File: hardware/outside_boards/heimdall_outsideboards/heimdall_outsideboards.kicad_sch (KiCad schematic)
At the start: 33 parts, among them IC1 CLRC66303HNY, J1 Motherboard, J2 LED Out, Y1 27.12MHz

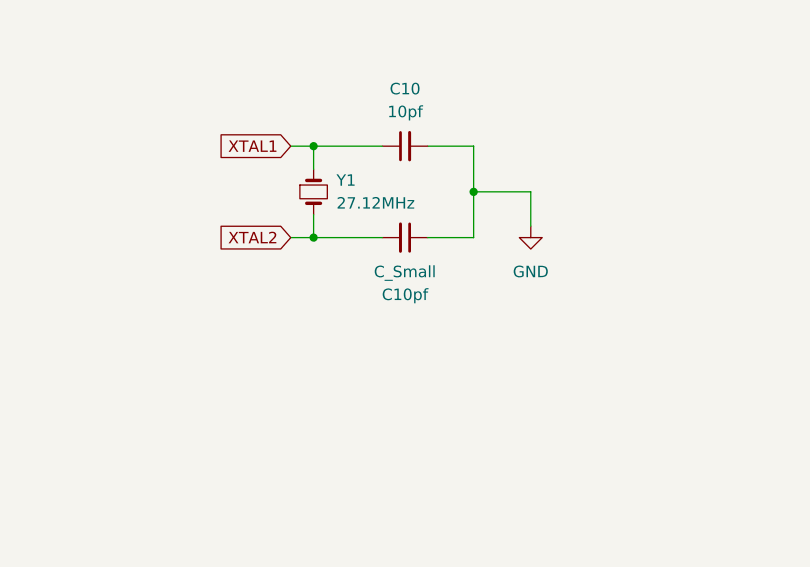
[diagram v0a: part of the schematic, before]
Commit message: Finished adding footprints
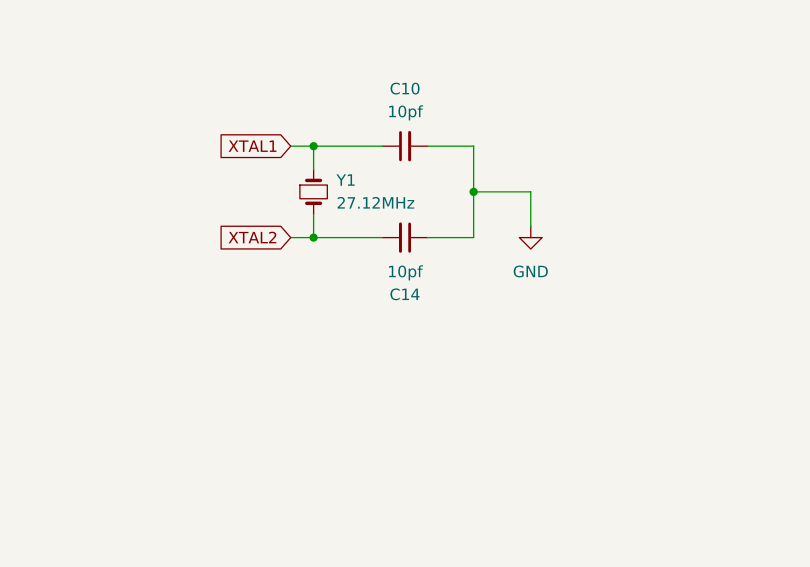
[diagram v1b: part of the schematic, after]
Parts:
- C14: renamed from C10pf; value C_Small -> 10pf
- J1: footprint (none) -> Connector_PinHeader_2.54mm:PinHeader_1x09_P2.54mm_Vertical
- J2: footprint (none) -> Connector_PinHeader_2.54mm:PinHeader_1x03_P2.54mm_Vertical
- TP1: footprint (none) -> TestPoint:TestPoint_Pad_D1.5mm
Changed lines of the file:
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@@
 			)
 		)
-		(property "Footprint" ""
+		(property "Footprint" "Connector_PinHeader_2.54mm:PinHeader_1x09_P2.54mm_Vertical"
 			(at 22.86 161.29 0)
 			(effects
@@
 		(on_board yes)
 		(dnp no)
-		(property "Reference" "C10pf"
+		(property "Reference" "C14"
 			(at 198.1137 157.48 90)
 			(effects
@@
 			)
 		)
-		(property "Value" "C_Small"
+		(property "Value" "10pf"
 			(at 198.1137 154.94 90)
 			(effects
@@
 			(project "heimdall_outsideboards"
 				(path "/5c087b52-dc4f-4954-b9fe-1d3bf0424550"
-					(reference "C10pf")
+					(reference "C14")
 					(unit 1)
 				)
@@
 			)
 		)
-		(property "Footprint" ""
+		(property "Footprint" "TestPoint:TestPoint_Pad_D1.5mm"
 			(at 233.68 86.36 0)
 			(effects
@@
 			)
 		)
-		(property "Footprint" ""
+		(property "Footprint" "Connector_PinHeader_2.54mm:PinHeader_1x03_P2.54mm_Vertical"
 			(at 22.86 186.69 0)
 			(effects

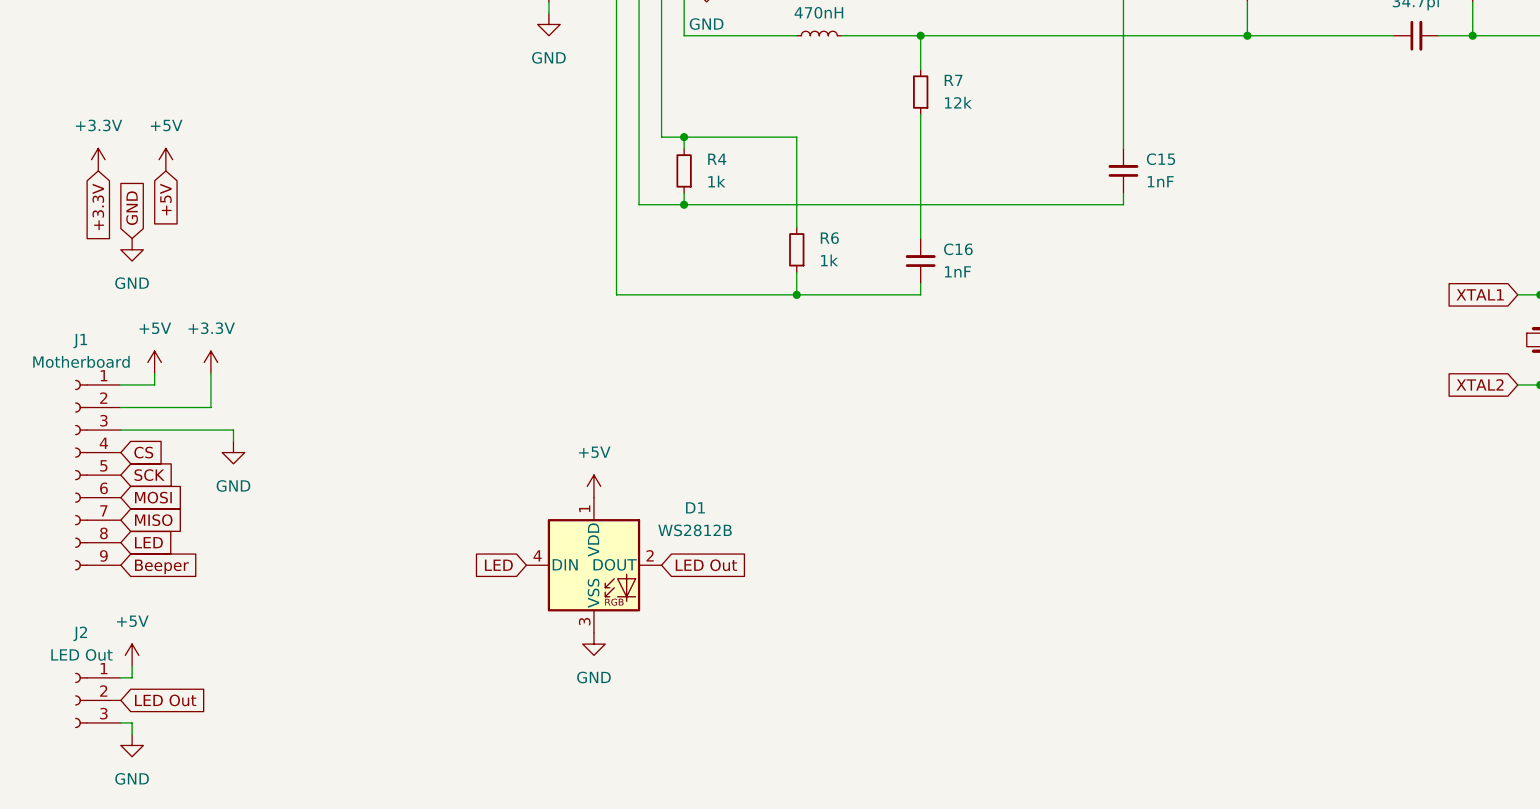
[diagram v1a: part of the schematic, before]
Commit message: Added a buzzer
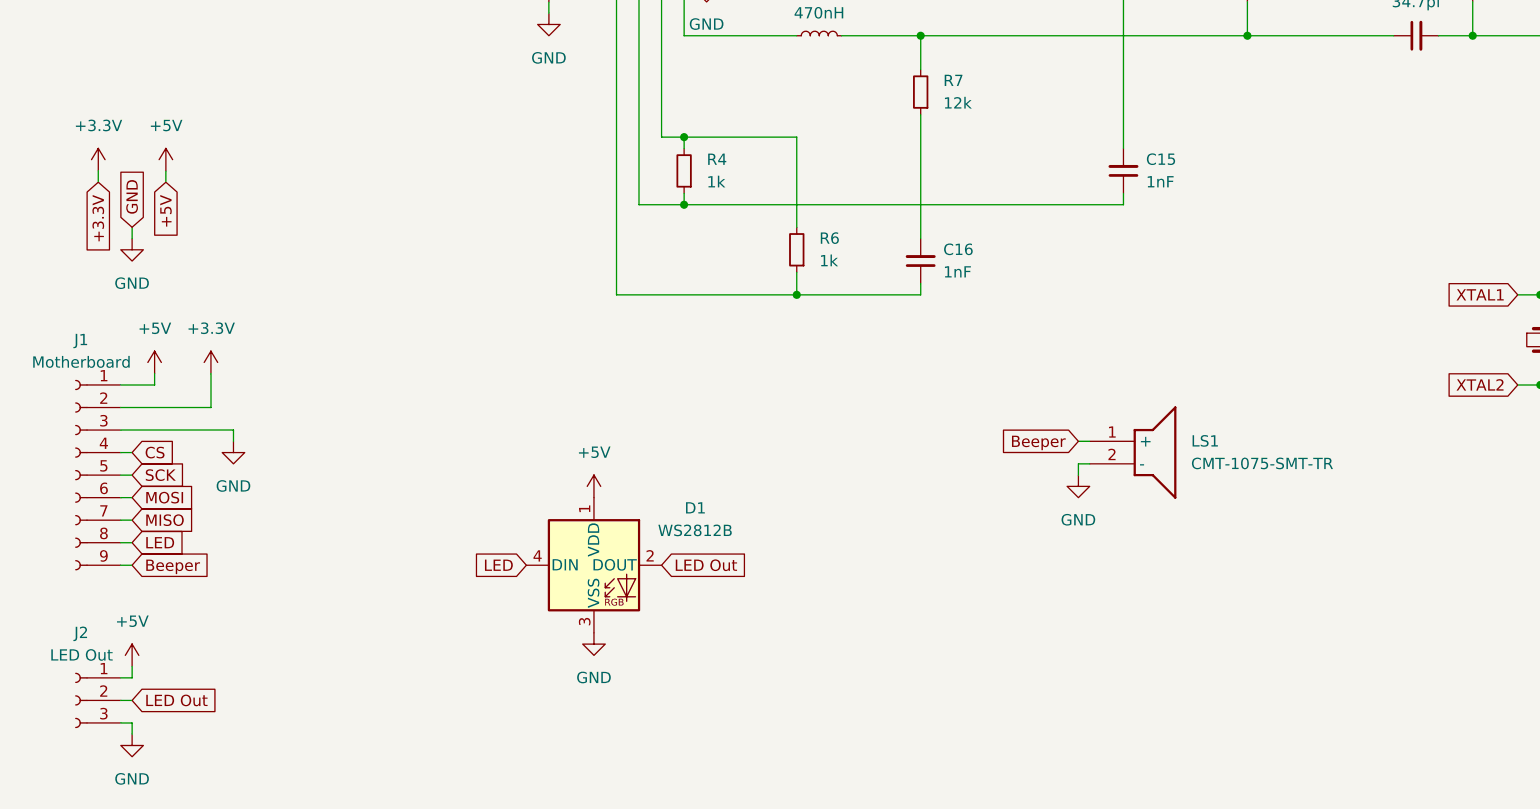
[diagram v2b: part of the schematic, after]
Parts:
- added LS1: CMT-1075-SMT-TR, CMT1075SMTTR, symbol CMT-1075-SMT-TR:CMT-1075-SMT-TR
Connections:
- net Beeper: now also LS1.1 (+)
- net GND: now also LS1.2 (-)
